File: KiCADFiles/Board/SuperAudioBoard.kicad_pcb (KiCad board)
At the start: 2 copper layers, 94 x 63 mm, 180 parts, among them J1 XLR, J10 5k Log Pot, J2 MONO JACK, J3 Barrel_Jack_PTH, J4 MONO JACK, J5 MONO JACK, J6 MONO JACK, J7 MONO JACK, J8 5k Log Pot, J9 5k Log Pot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

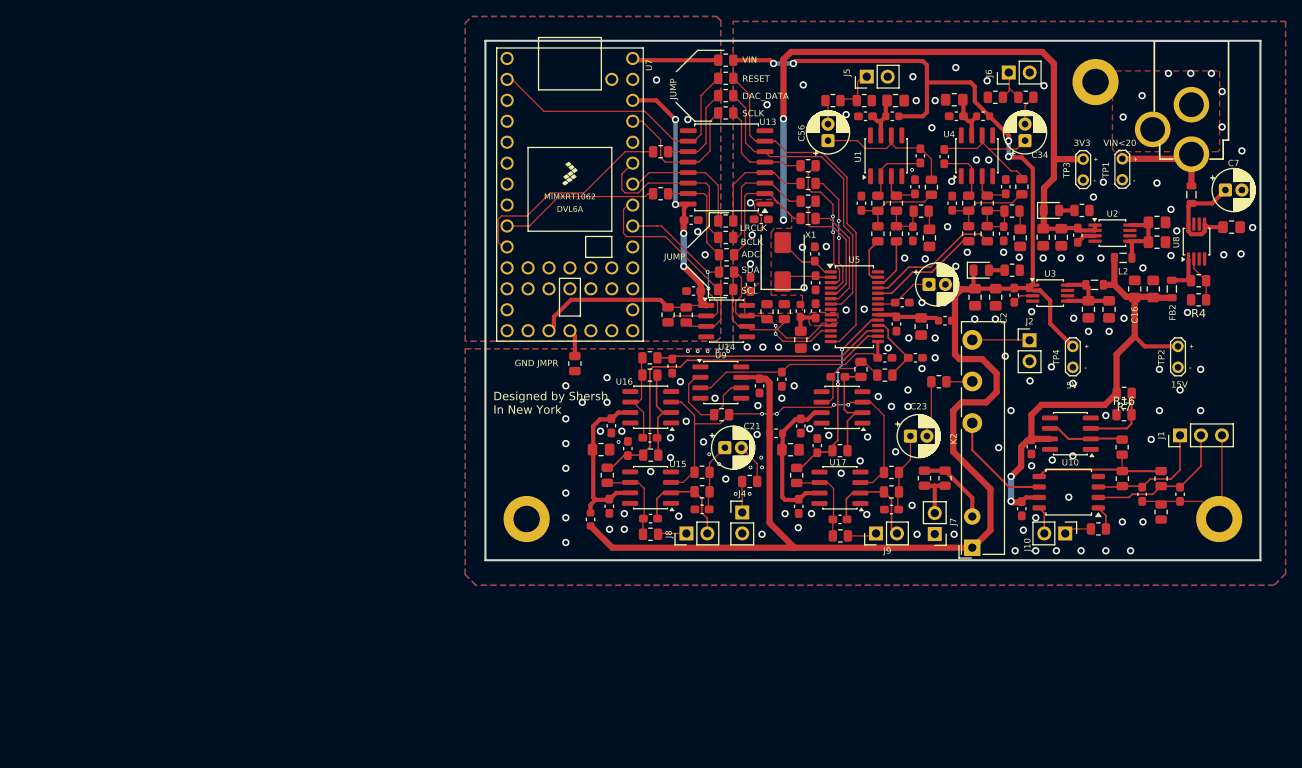
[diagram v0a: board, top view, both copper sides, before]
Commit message: improved layout for noise immunity
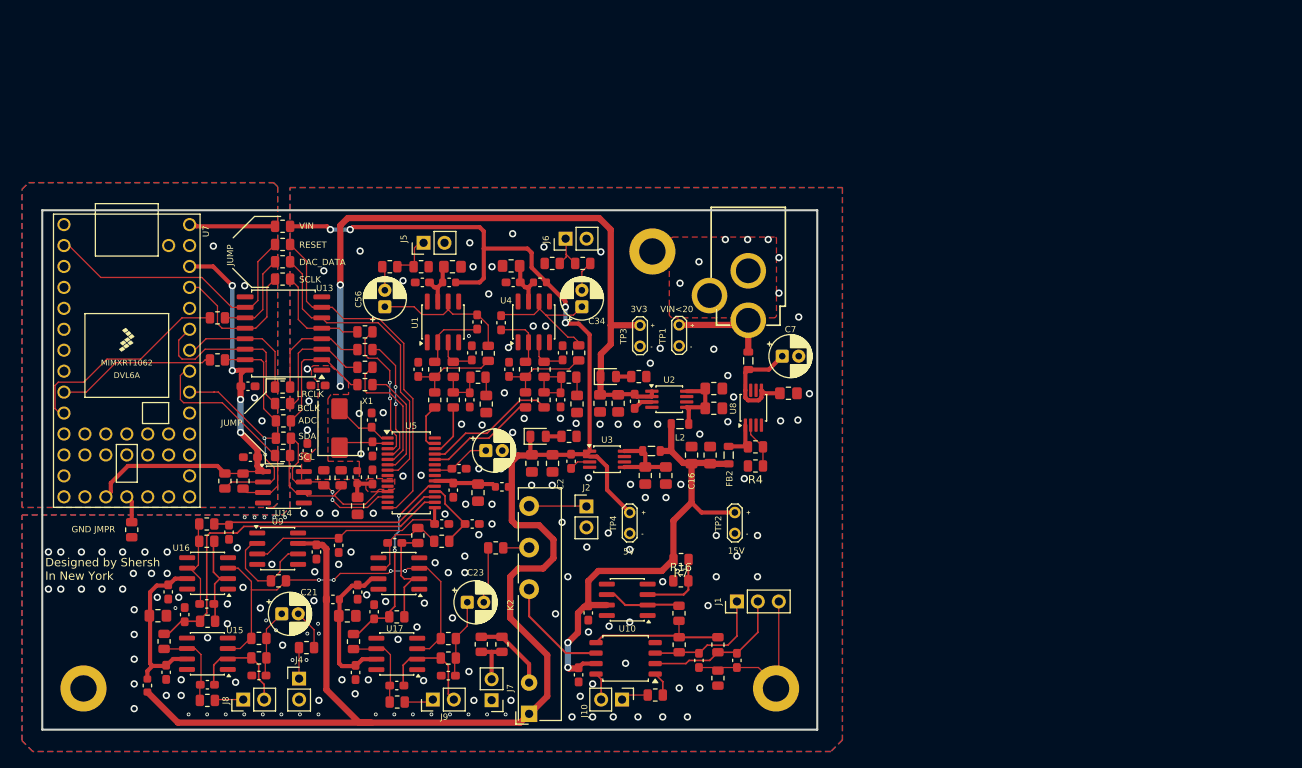
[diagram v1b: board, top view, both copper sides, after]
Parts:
- moved H3 57.5 mm to (170.5, 81.7)
- moved H1 57.5 mm to (101.5, 134.7)
- moved H2 57.5 mm to (185.5, 134.7)
- moved U16 57.4 mm to (116.5, 120.7)
- moved U9 57.4 mm to (125.0, 117.8)
- moved R67 57.4 mm to (116.5, 126.5)
- moved C1 57.4 mm to (164.2, 100.1)
- moved C11 57.4 mm to (169.6, 108.9)
- moved C12 57.4 mm to (177.9, 98.3)
- moved C13 57.4 mm to (172.1, 108.9)
- moved C14 57.4 mm to (153.1, 96.0)
- moved C15 57.4 mm to (149.2, 90.2)
- moved C16 57.4 mm to (175.2, 106.4)
- moved C17 57.4 mm to (177.5, 106.4)
- moved C2 57.4 mm to (158.4, 107.4)
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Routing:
- net +5VA: track 202.5 -> 206.4 mm
- net GNDPWR: track 20.8 -> 21.6 mm
- net GND: vias 156 -> 182

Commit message: added LED driver JST connector
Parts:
- added J12: Conn_01x06, Connector_JST:JST_EH_B6B-EH-A_1x06_P2.50mm_Vertical, F.Cu at (97.1, 117.6)
- moved R55 6.74 mm to (113.7, 113.2)
- moved U7 3.15 mm to (103.6, 95.0)
- moved H1 3.00 mm to (98.5, 134.7)
- moved C76 2.75 mm to (118.7, 97.9), turned to 180 degrees
- moved R35 1.35 mm to (116.4, 94.8)
- moved R56 1.25 mm to (116.5, 89.8)
- moved R58 0.84 mm to (118.6, 108.7)
- moved C75 0.21 mm to (121.6, 106.8)
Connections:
- U7 pad 13: unconnected-(U7-11_MOSI_CTX1-Pad13) -> /TeensyAndDigital/LED_SR_SDI
- U7 pad 14: unconnected-(U7-12_MISO_MQSL-Pad14) -> /TeensyAndDigital/LED_SR_SDO
- U7 pad 20: unconnected-(U7-13_SCK_CRX1_LED-Pad20) -> /TeensyAndDigital/LED_SR_CLK
- U7 pad 21: unconnected-(U7-14_A0_TX3_SPDIF_OUT-Pad21) -> /TeensyAndDigital/LED_SR_LATCH
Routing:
- net /TeensyAndDigital/LED_SR_SDO: track 0.00 -> 21.8 mm, vias 0 -> 2
- net /TeensyAndDigital/LED_SR_SDI: track 0.00 -> 19.2 mm
- net /TeensyAndDigital/LED_SR_LATCH: track 0.00 -> 14.2 mm
- net /TeensyAndDigital/LED_SR_CLK: track 0.00 -> 14.1 mm
- net /TeensyAndDigital/T_3.3V: track 53.4 -> 67.2 mm
- net Net-(U7-8_TX2_IN1): track 26.6 -> 32.7 mm
- net DGND: track 3.33 -> 0.00 mm, vias 4 -> 15
- net /TeensyAndDigital/T_SCL: track 27.2 -> 30.5 mm
- net /TeensyAndDigital/T_VIN: track 10.5 -> 13.6 mm
- net /TeensyAndDigital/T_LRCLK: track 15.9 -> 19.1 mm
- net /TeensyAndDigital/T_CODEC_RESET: track 34.6 -> 37.8 mm
- net /TeensyAndDigital/T_SDA: track 24.7 -> 27.6 mm
- net /TeensyAndDigital/T_SCLK: track 18.3 -> 21.1 mm
- net /TeensyAndDigital/T_ADC_DATA: track 12.2 -> 13.9 mm
- net /TeensyAndDigital/T_DAC_DATA: track 11.1 -> 12.7 mm
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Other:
- board size 94 x 63 mm -> 97 x 63 mm
- board text added: "CLK"
- board text added: "GND"
- board text added: "GND JMP"
- board text added: "LE"
- board text added: "SDI"
- board text added: "SDO"
- board text removed: "GND JMPR"
- board text removed: "JUMP"
